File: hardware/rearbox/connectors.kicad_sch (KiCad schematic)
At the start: 2 parts, among them J3 Conn_02x28_Top_Bottom, J4 Auxiliary

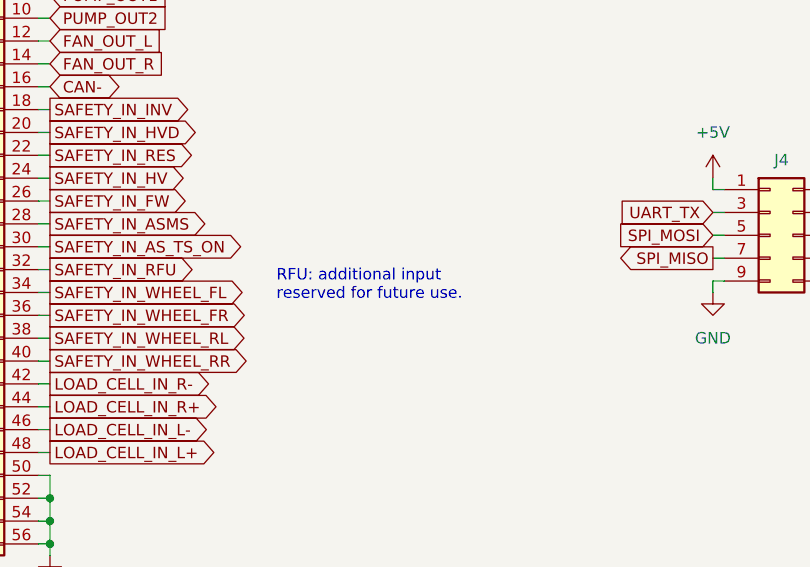
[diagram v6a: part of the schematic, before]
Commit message: Fix measurement bridges polarity
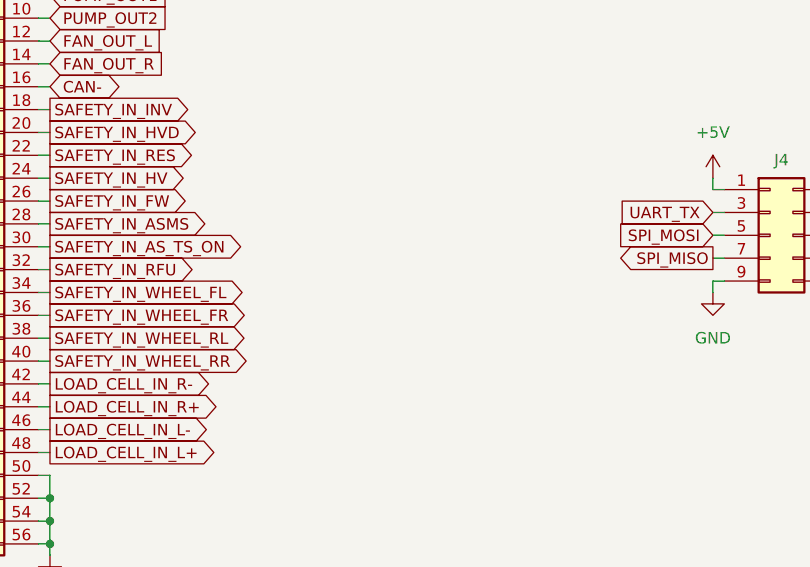
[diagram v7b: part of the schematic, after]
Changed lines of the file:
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@@
   (title_block
     (title "Connectors")
-    (date "2023-11-17")
+    (date "2024-04-28")
     (rev "${REVISION}")
     (company "Author: I. Kajdan")
@@
     (effects (font (size 1.27 1.27)) (justify right))
   )
-  (text_box "RFU: additional input reserved for future use."
-    (at 146.05 102.87 0) (size 29.21 5.08)
-    (stroke (width -0.0001) (type default))
-    (fill (type none))
-    (effects (font (size 1.27 1.27)) (justify left top))
-  )
   (global_label "WATER_PRESSURE_IN1" (shape output) (at 106.68 99.06 180) (fields_autoplaced)
     (effects (font (size 1.27 1.27) (color 0 132 132 1)) (justify right))
@@
   (symbol (lib_id "power:+5V") (at 195.58 93.98 0) (unit 1)
     (in_bom yes) (on_board yes) (dnp no)
-    (property "Reference" "#PWR056" (at 195.58 97.79 0)
+    (property "Reference" "#PWR057" (at 195.58 97.79 0)
       (effects (font (size 1.27 1.27)) hide)
     )
@@
       (project "rearbox"
         (path "/b652b05a-4e3d-4ad1-b032-18886abe7d45/cf65c657-8245-46fb-8929-d241bd579513"
-          (reference "#PWR056") (unit 1)
+          (reference "#PWR057") (unit 1)
         )
       )
@@
   (symbol (lib_id "Power_Ports:+5V_EXT") (at 106.68 91.44 90) (unit 1)
     (in_bom yes) (on_board yes) (dnp no)
-    (property "Reference" "#PWR051" (at 110.49 91.44 0)
+    (property "Reference" "#PWR052" (at 110.49 91.44 0)
       (effects (font (size 1.27 1.27)) hide)
     )
@@
       (project "rearbox"
         (path "/b652b05a-4e3d-4ad1-b032-18886abe7d45/cf65c657-8245-46fb-8929-d241bd579513"
-          (reference "#PWR051") (unit 1)
+          (reference "#PWR052") (unit 1)
         )
       )
@@
   (symbol (lib_id "power:+3.3V") (at 210.82 93.98 0) (unit 1)
     (in_bom yes) (on_board yes) (dnp no)
-    (property "Reference" "#PWR058" (at 210.82 97.79 0)
+    (property "Reference" "#PWR059" (at 210.82 97.79 0)
       (effects (font (size 1.27 1.27)) hide)
     )
@@
       (project "rearbox"
         (path "/b652b05a-4e3d-4ad1-b032-18886abe7d45/cf65c657-8245-46fb-8929-d241bd579513"
-          (reference "#PWR058") (unit 1)
+          (reference "#PWR059") (unit 1)
         )
       )
@@
   (symbol (lib_id "power:GND") (at 195.58 106.68 0) (unit 1)
     (in_bom yes) (on_board yes) (dnp no) (fields_autoplaced)
-    (property "Reference" "#PWR057" (at 195.58 113.03 0)
+    (property "Reference" "#PWR058" (at 195.58 113.03 0)
       (effects (font (size 1.27 1.27)) hide)
     )
@@
       (project "rearbox"
         (path "/b652b05a-4e3d-4ad1-b032-18886abe7d45/cf65c657-8245-46fb-8929-d241bd579513"
-          (reference "#PWR057") (unit 1)
+          (reference "#PWR058") (unit 1)
         )
       )
@@
   (symbol (lib_id "power:GND") (at 121.92 135.89 0) (mirror y) (unit 1)
     (in_bom yes) (on_board yes) (dnp no) (fields_autoplaced)
-    (property "Reference" "#PWR055" (at 121.92 142.24 0)
+    (property "Reference" "#PWR056" (at 121.92 142.24 0)
       (effects (font (size 1.27 1.27)) hide)
     )
@@
       (project "rearbox"
         (path "/b652b05a-4e3d-4ad1-b032-18886abe7d45/cf65c657-8245-46fb-8929-d241bd579513"
-          (reference "#PWR055") (unit 1)
+          (reference "#PWR056") (unit 1)
         )
       )
@@
   (symbol (lib_id "power:+24V") (at 106.68 64.77 0) (unit 1)
     (in_bom yes) (on_board yes) (dnp no)
-    (property "Reference" "#PWR050" (at 106.68 68.58 0)
+    (property "Reference" "#PWR051" (at 106.68 68.58 0)
       (effects (font (size 1.27 1.27)) hide)
     )
@@
       (project "rearbox"
         (path "/b652b05a-4e3d-4ad1-b032-18886abe7d45/cf65c657-8245-46fb-8929-d241bd579513"
-          (reference "#PWR050") (unit 1)
+          (reference "#PWR051") (unit 1)
         )
       )
@@
   (symbol (lib_id "Power_Ports:+3V_EXT") (at 106.68 116.84 90) (unit 1)
     (in_bom yes) (on_board yes) (dnp no)
-    (property "Reference" "#PWR052" (at 101.6 116.84 0)
+    (property "Reference" "#PWR053" (at 101.6 116.84 0)
       (effects (font (size 1.27 1.27)) hide)
     )
@@
       (project "rearbox"
         (path "/b652b05a-4e3d-4ad1-b032-18886abe7d45/cf65c657-8245-46fb-8929-d241bd579513"
-          (reference "#PWR052") (unit 1)
+          (reference "#PWR053") (unit 1)
         )
       )
@@
   (symbol (lib_id "power:GND") (at 106.68 135.89 0) (mirror y) (unit 1)
     (in_bom yes) (on_board yes) (dnp no) (fields_autoplaced)
-    (property "Reference" "#PWR053" (at 106.68 142.24 0)
+    (property "Reference" "#PWR054" (at 106.68 142.24 0)
       (effects (font (size 1.27 1.27)) hide)
     )
@@
       (project "rearbox"
         (path "/b652b05a-4e3d-4ad1-b032-18886abe7d45/cf65c657-8245-46fb-8929-d241bd579513"
-          (reference "#PWR053") (unit 1)
+          (reference "#PWR054") (unit 1)
         )
       )
@@
   (symbol (lib_id "power:+24V") (at 121.92 64.77 0) (unit 1)
     (in_bom yes) (on_board yes) (dnp no)
-    (property "Reference" "#PWR054" (at 121.92 68.58 0)
+    (property "Reference" "#PWR055" (at 121.92 68.58 0)
       (effects (font (size 1.27 1.27)) hide)
     )
@@
       (project "rearbox"
         (path "/b652b05a-4e3d-4ad1-b032-18886abe7d45/cf65c657-8245-46fb-8929-d241bd579513"
-          (reference "#PWR054") (unit 1)
-        )
-      )
+          (reference "#PWR055") (unit 1)
+        )
+      )
